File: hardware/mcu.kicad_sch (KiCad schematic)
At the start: 8 parts, among them J4 DebugEdge_02x03, SW1 RESET, U1 STM32G070CBTx_u, X1 KC2520Z

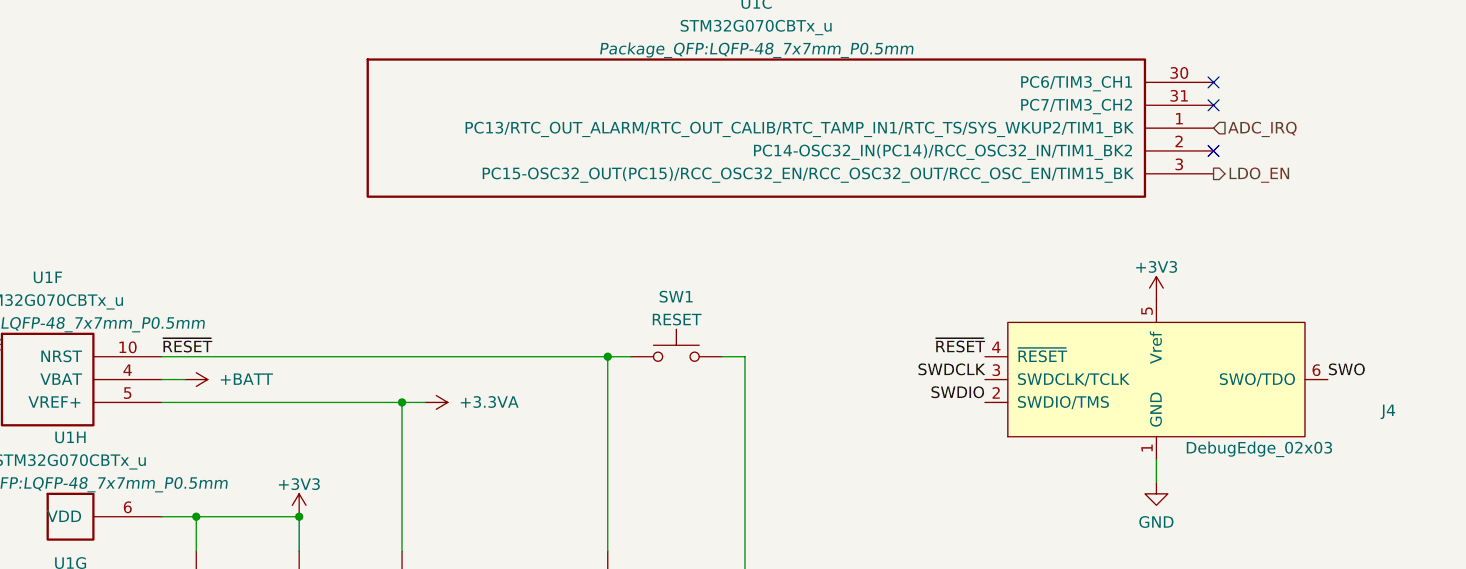
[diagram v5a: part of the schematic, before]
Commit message: Realized that 5V to VBat pin would fry the uC and abandoned ultra-low power design. Deferred to next revision.
A
A
A
A
A
A
A
A
A
A
A
A
A
A
A
A
A
A
B
B
B
B
B
B
B
B
B
B
B
B
B
B
B
A
A
A
A
A
A
A
A
A
A
A
A
A
A
P
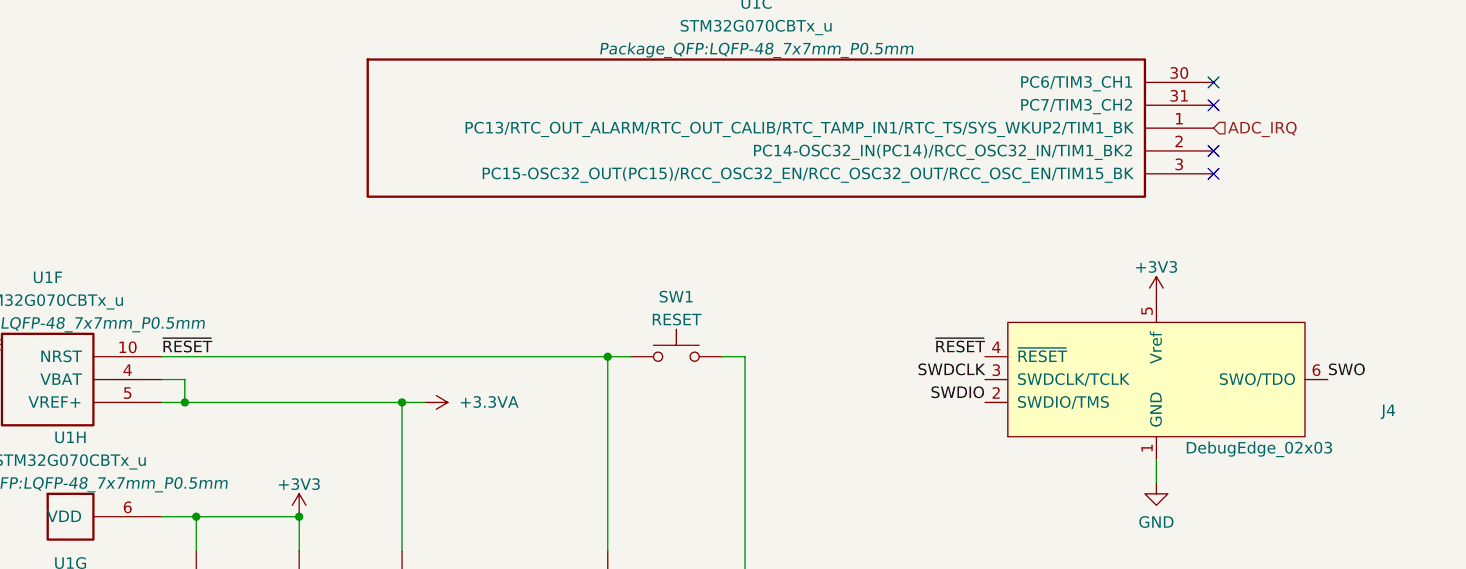
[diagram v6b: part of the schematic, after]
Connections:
- net +BATT is gone; now on net +3.3VA: U1.4 (VBAT)
- net LDO_EN: no longer names the net of U1.3 (PC15-OSC32_OUT(PC15)/RCC_OSC32_EN/RCC_OSC32_OUT/RCC_OSC_EN/TIM15_BK)
- no-connect marks 6 -> 7
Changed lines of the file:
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@@
+	)
+	(junction
+		(at 115.57 149.86)
+		(diameter 0)
+		(color 0 0 0 0)
 	)
 	(junction
@@
 	)
 	(no_connect
+		(at 229.87 124.46)
+	)
+	(no_connect
 		(at 127 69.85)
 	)
@@
 		)
 	)
+	(wire
+		(pts
+			(xy 115.57 147.32) (xy 115.57 149.86)
+		)
+		(stroke
+			(width 0)
+			(type default)
+		)
+	)
 	(bus
 		(pts
@@
 	(wire
 		(pts
+			(xy 115.57 149.86) (xy 113.03 149.86)
+		)
+		(stroke
+			(width 0)
+			(type default)
+		)
+	)
+	(wire
+		(pts
 			(xy 113.03 147.32) (xy 115.57 147.32)
 		)
@@
 	(wire
 		(pts
-			(xy 139.7 149.86) (xy 113.03 149.86)
+			(xy 139.7 149.86) (xy 115.57 149.86)
 		)
 		(stroke
@@
 		(shape input)
 		(at 127 74.93 0)
-		(effects
-			(font
-				(size 1.27 1.27)
-			)
-			(justify left)
-		)
-	)
-	(hierarchical_label "LDO_EN"
-		(shape output)
-		(at 229.87 124.46 0)
 		(effects
 			(font
@@
 				)
 			)
-		)
-	)
-	(symbol
-		(lib_id "power:+BATT")
-		(at 115.57 147.32 270)
-		(unit 1)
-		(exclude_from_sim no)
-		(in_bom yes)
-		(on_board yes)
-		(dnp no)
-		(fields_autoplaced yes)
-		(property "Reference" "#PWR04"
-			(at 111.76 147.32 0)
-			(effects
-				(font
-					(size 1.27 1.27)
-				)
-				(hide yes)
-			)
-		)
-		(property "Value" "+BATT"
-			(at 119.38 147.3199 90)
-			(effects
-				(font
-					(size 1.27 1.27)
-				)
-				(justify left)
-			)
-		)
-		(property "Footprint" ""
-			(at 115.57 147.32 0)
-			(effects
-				(font
-					(size 1.27 1.27)
-				)
-				(hide yes)
-			)
-		)
-		(property "Datasheet" ""
-			(at 115.57 147.32 0)
-			(effects
-				(font
-					(size 1.27 1.27)
-				)
-				(hide yes)
-			)
-		)
-		(property "Description" "Power symbol creates a global label with name \"+BATT\""
-			(at 115.57 147.32 0)
-			(effects
-				(font
-					(size 1.27 1.27)
-				)
-				(hide yes)
-			)
-		)
-		(pin "1"
-		)
-		(instances
-			(project ""
-				(path "/adf38c8f-bada-4838-acc6-e6af19946742/e50b7c46-7cda-4158-8fd2-26ea52f7127e"
-					(reference "#PWR04")
-					(unit 1)
-				)
-			)

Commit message: Some more routing
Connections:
- net GPIO_PB5: no longer U1.45 (PB6/I2C1_SCL/SPI2_MISO/TIM16_CH1N/TIM1_CH3/USART1_TX)
- net GPIO_PA8: no longer names the net of U1.28 (PA8/RCC_MCO/SPI2_NSS/TIM1_CH1)
- new net GPIO_PB6: U1.45 (PB6/I2C1_SCL/SPI2_MISO/TIM16_CH1N/TIM1_CH3/USART1_TX)
- no-connect marks 7 -> 8
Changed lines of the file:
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@@
 		(at 229.87 121.92)
+	)
+	(no_connect
+		(at 127 80.01)
 	)
 	(bus_entry
@@
 		)
 	)
-	(hierarchical_label "GPIO_PB5"
+	(hierarchical_label "GPIO_PB6"
 		(shape bidirectional)
 		(at 78.74 133.35 0)
@@
 		(effects
 			(font
-				(size 1.27 1.27)
-			)
-			(justify left)
-		)
-	)
-	(hierarchical_label "GPIO_PA8"
-		(shape bidirectional)
-		(at 127 80.01 0)
-		(effects
-			(font

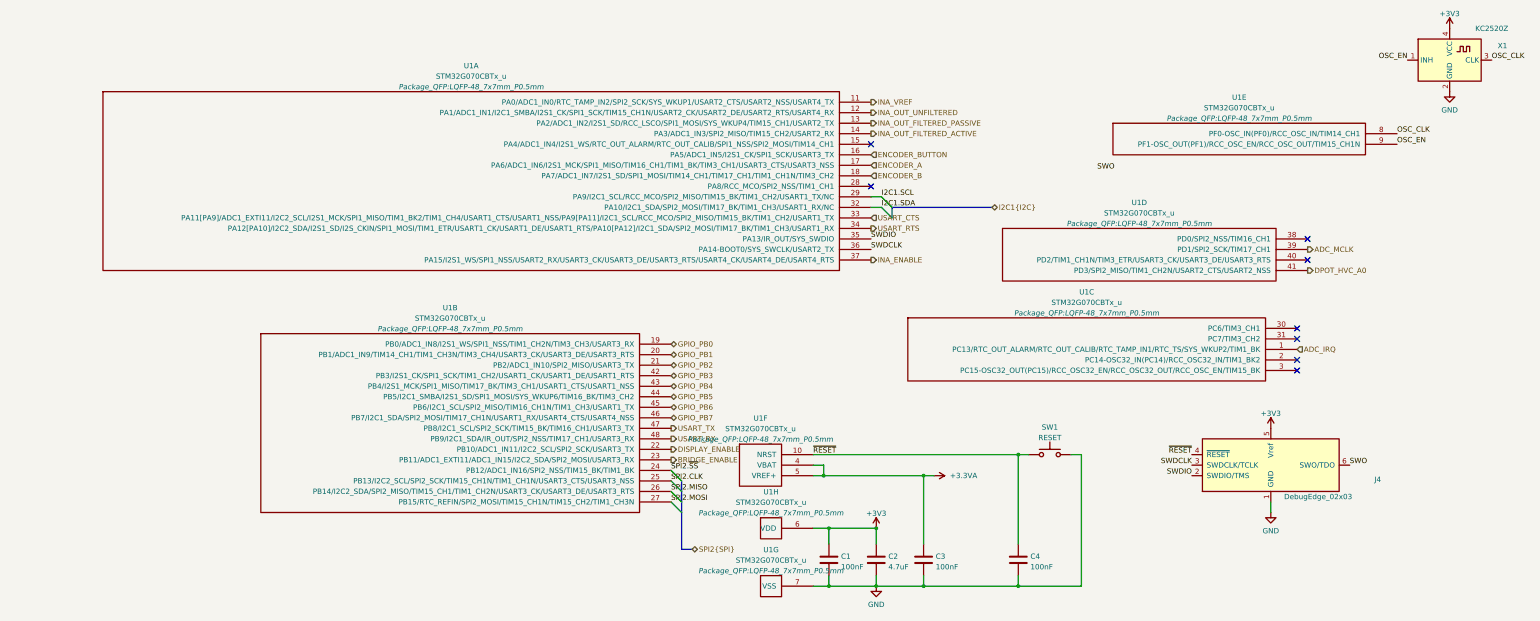
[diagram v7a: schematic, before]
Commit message: Ran electrical check on schematic and implemented corrections
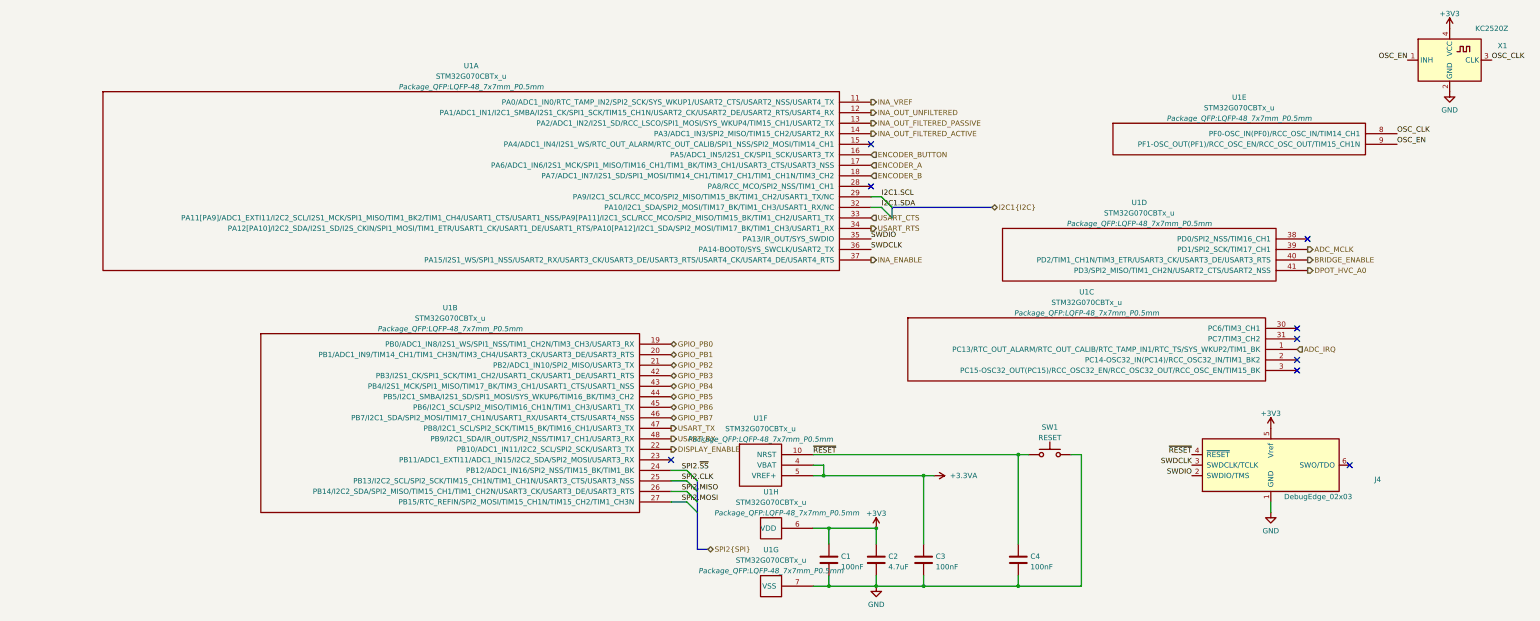
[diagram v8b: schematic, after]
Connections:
- net BRIDGE_ENABLE: now also U1.40 (PD2/TIM1_CH1N/TIM3_ETR/USART3_CK/USART3_DE/USART3_RTS); no longer U1.23 (PB11/ADC1_EXTI11/ADC1_IN15/I2C2_SDA/SPI2_MOSI/USART3_RX)
- net SWO: no longer names the net of J4.6 (SWO/TDO)
- no-connect marks 8 -> 9
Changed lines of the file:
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@@
+	)
+	(no_connect
+		(at 242.57 147.32)
 	)
 	(no_connect
@@
 	)
 	(no_connect
-		(at 232.41 97.79)
+		(at 78.74 146.05)
 	)
 	(no_connect
@@
 	)
 	(bus_entry
-		(at 81.28 156.21)
+		(at 85.09 156.21)
 		(size -2.54 -2.54)
 		(stroke
@@
 	)
 	(bus_entry
-		(at 78.74 151.13)
+		(at 82.55 151.13)
 		(size 2.54 2.54)
 		(stroke
@@
 	)
 	(bus_entry
-		(at 78.74 156.21)
+		(at 82.55 156.21)
 		(size 2.54 2.54)
 		(stroke
@@
 	)
 	(bus_entry
-		(at 78.74 148.59)
+		(at 82.55 148.59)
 		(size 2.54 2.54)
 		(stroke
@@
 	(wire
 		(pts
+			(xy 78.74 148.59) (xy 82.55 148.59)
+		)
+		(stroke
+			(width 0)
+			(type default)
+		)
+	)
+	(wire
+		(pts
 			(xy 113.03 162.56) (xy 116.84 162.56)
 		)
@@
 	(bus
 		(pts
-			(xy 81.28 158.75) (xy 81.28 167.64)
+			(xy 85.09 158.75) (xy 85.09 167.64)
 		)
 		(stroke
@@
 	(bus
 		(pts
-			(xy 81.28 156.21) (xy 81.28 158.75)
+			(xy 85.09 156.21) (xy 85.09 158.75)
 		)
 		(stroke
@@
 	(bus
 		(pts
-			(xy 81.28 153.67) (xy 81.28 156.21)
+			(xy 85.09 153.67) (xy 85.09 156.21)
 		)
 		(stroke
@@
 	(bus
 		(pts
-			(xy 81.28 151.13) (xy 81.28 153.67)
+			(xy 85.09 151.13) (xy 85.09 153.67)
 		)
 		(stroke
@@
 	(wire
 		(pts
+			(xy 78.74 153.67) (xy 82.55 153.67)
+		)
+		(stroke
+			(width 0)
+			(type default)
+		)
+	)
+	(wire
+		(pts
 			(xy 165.1 144.78) (xy 162.56 144.78)
 		)
@@
 	(wire
 		(pts
+			(xy 78.74 156.21) (xy 82.55 156.21)
+		)
+		(stroke
+			(width 0)
+			(type default)
+		)
+	)
+	(wire
+		(pts
 			(xy 128.27 162.56) (xy 128.27 166.37)
 		)
@@
 	(bus
 		(pts
-			(xy 81.28 167.64) (xy 83.82 167.64)
+			(xy 85.09 167.64) (xy 87.63 167.64)
 		)
 		(stroke
@@
 		(pts
 			(xy 139.7 149.86) (xy 115.57 149.86)
+		)
+		(stroke
+			(width 0)
+			(type default)
+		)
+	)
+	(wire
+		(pts
+			(xy 78.74 151.13) (xy 82.55 151.13)
 		)
 		(stroke
@@
 	)
 	(label "SPI2.MOSI"
-		(at 78.74 156.21 0)
+		(at 81.28 156.21 0)
 		(effects
 			(font
@@
 	)
 	(label "SPI2.CLK"
-		(at 78.74 151.13 0)
+		(at 81.28 151.13 0)
 		(effects
 			(font
@@
 	)
 	(label "SPI2.~{SS}"
-		(at 78.74 148.59 0)
+		(at 81.28 148.59 0)
 		(effects
 			(font
@@
 		)
 	)
-	(label "SWO"
-		(at 242.57 147.32 0)
-		(effects
-			(font
-				(size 1.27 1.27)
-			)
-			(justify left bottom)
-		)
-	)
 	(label "~{RESET}"
 		(at 204.47 144.78 180)
@@
 		)
 	)
-	(label "SWO"
-		(at 181.61 76.2 0)
-		(effects
-			(font
-				(size 1.27 1.27)
-			)
-			(justify left bottom)
-		)
-	)
 	(label "I2C1.SCL"
 		(at 129.54 82.55 0)
@@
 	)
 	(label "SPI2.MISO"
-		(at 78.74 153.67 0)
+		(at 81.28 153.67 0)
 		(effects
 			(font
@@
 	(hierarchical_label "SPI2{SPI}"
 		(shape bidirectional)
-		(at 83.82 167.64 0)
+		(at 87.63 167.64 0)
 		(effects
 			(font
@@
 	(hierarchical_label "BRIDGE_ENABLE"
 		(shape output)
-		(at 78.74 146.05 0)
+		(at 232.41 97.79 0)
 		(effects
 			(font
@@
 		(on_board yes)
 		(dnp no)
-		(fields_autoplaced yes)
 		(property "Reference" "U1"
 			(at 102.87 153.7834 0)
@@
 		)
 		(property "Footprint" "Package_QFP:LQFP-48_7x7mm_P0.5mm"
-			(at 102.87 158.8572 0)
-			(effects
-				(font
+			(at 106.68 158.8572 0)
+			(effects
+				(font
